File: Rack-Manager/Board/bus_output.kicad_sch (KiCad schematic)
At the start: 28 parts, among them J3 TBP03R1-350-04BE, J4 TBP03R1-350-04BE, Q1 NTR4003NT1G, Q2 SiS435DNT, Q3 NTR4003NT1G, Q4 SiS435DNT, U10 INA3221

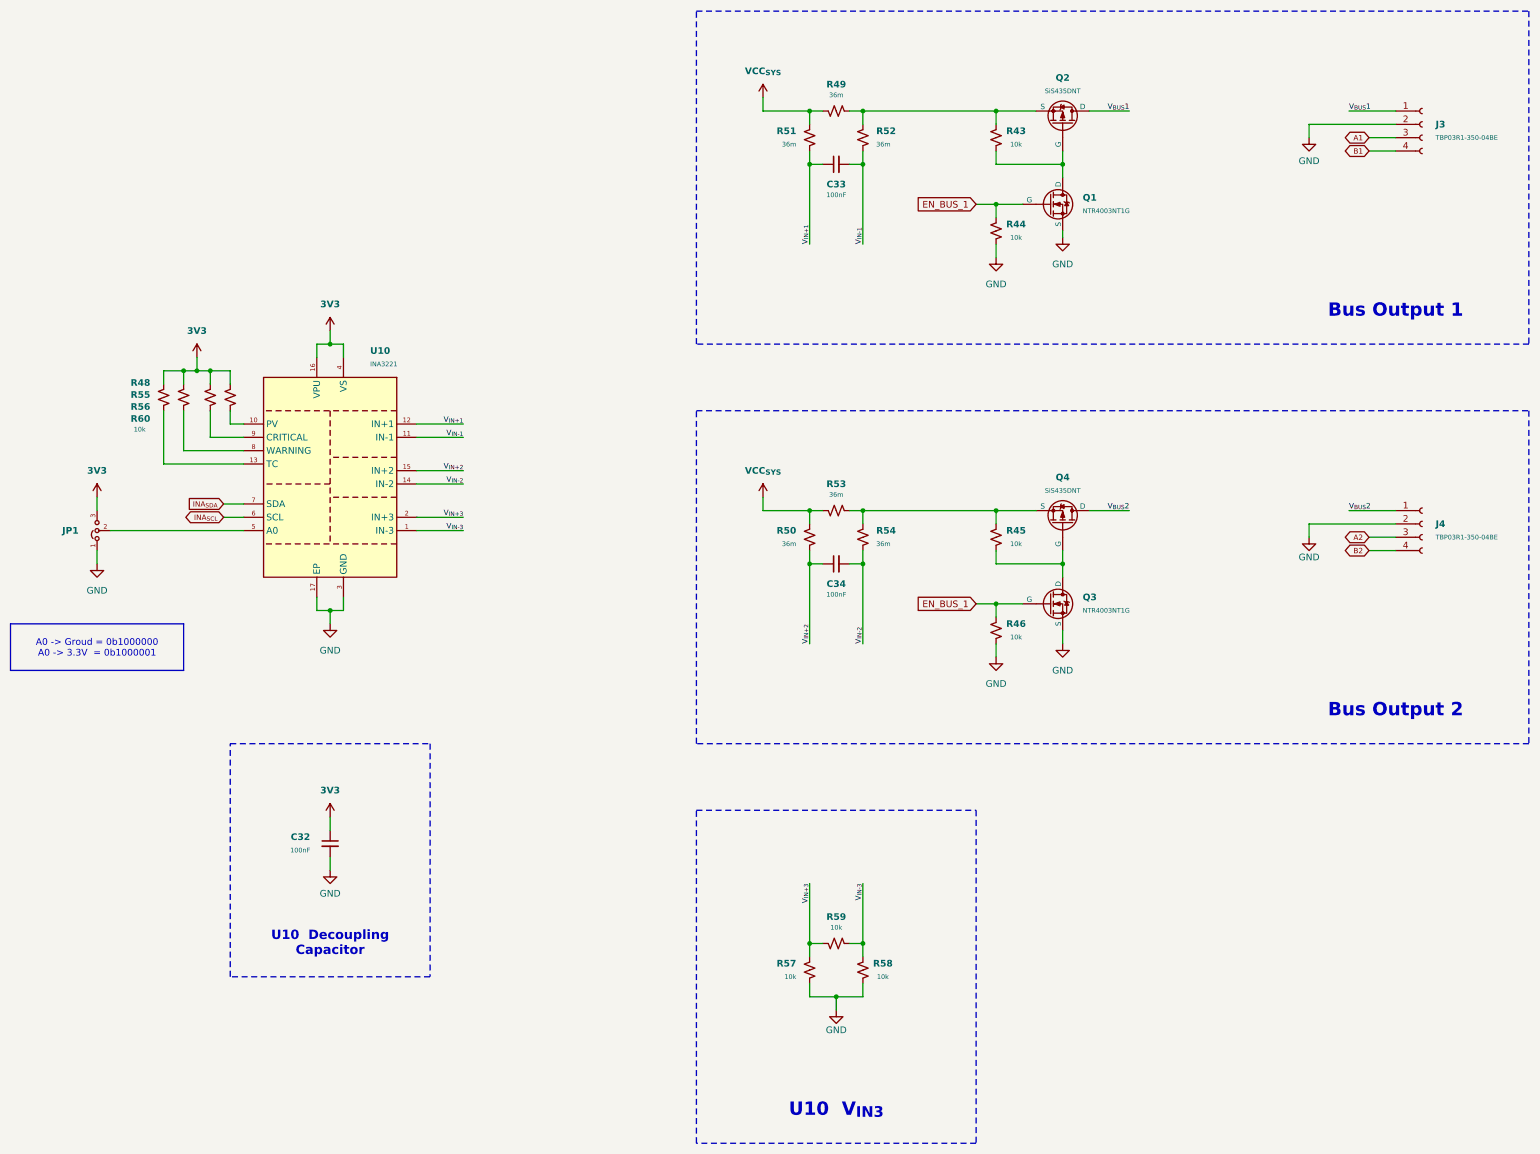
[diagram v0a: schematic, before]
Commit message: Added the fan management sheet and the mosfets for it
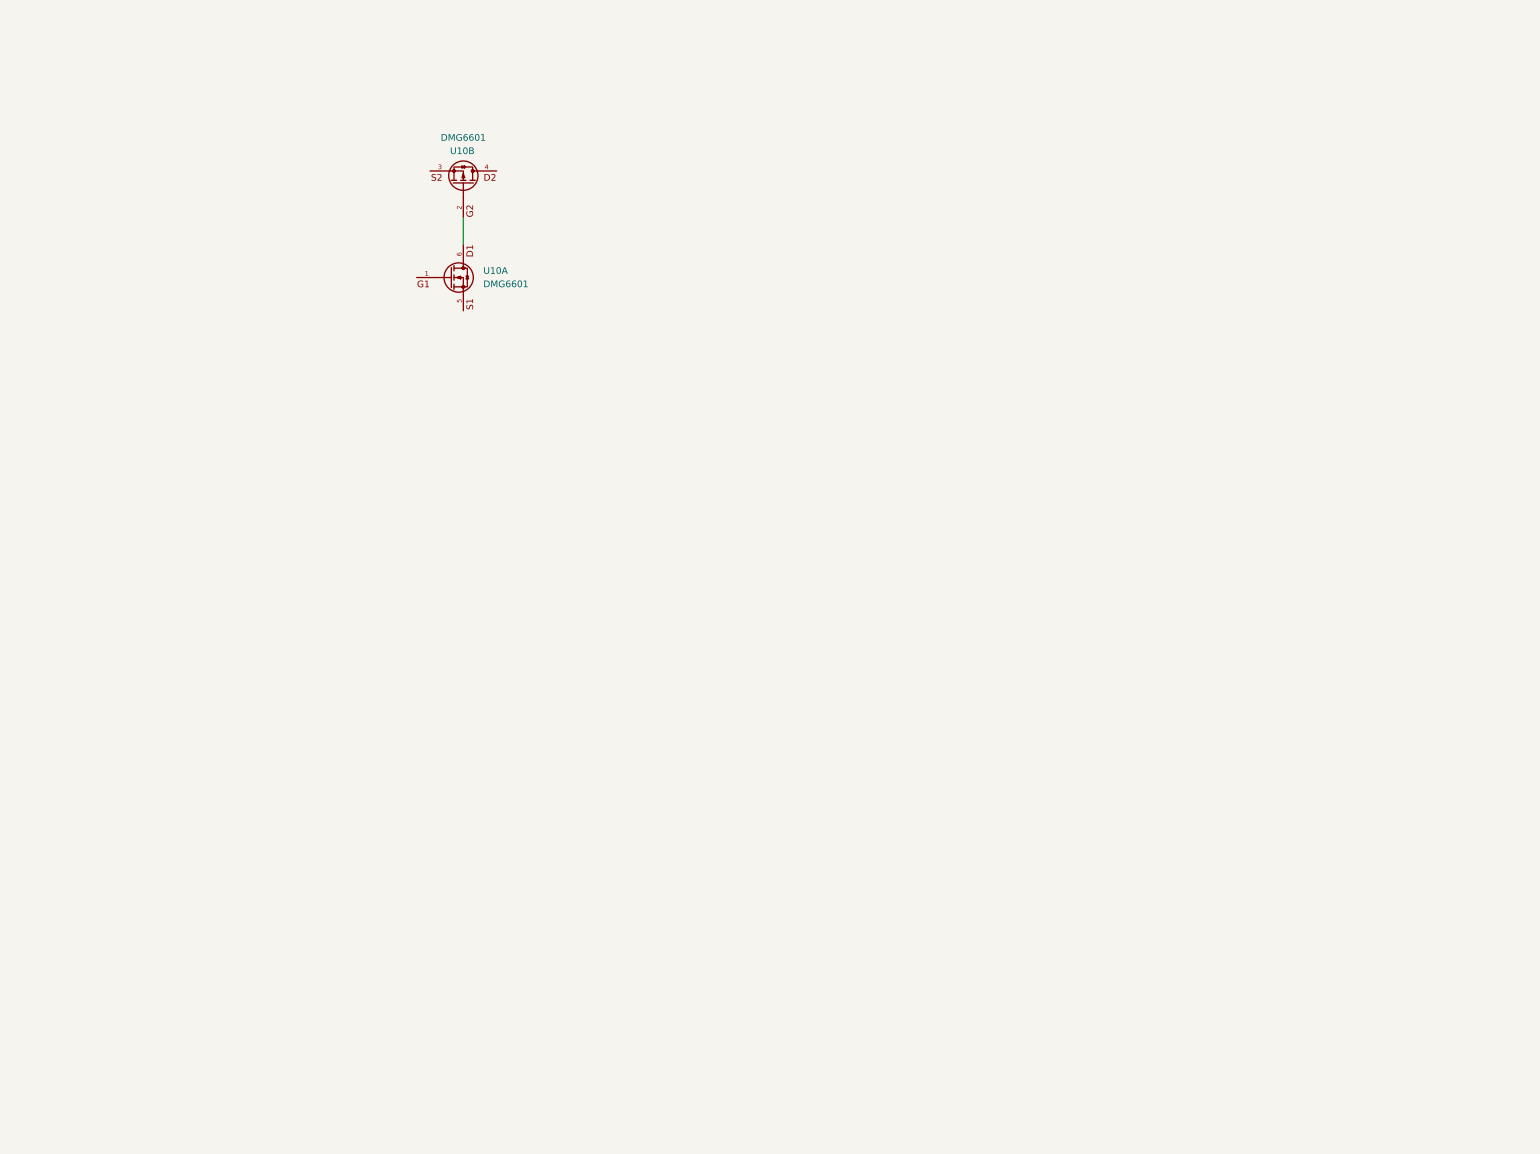
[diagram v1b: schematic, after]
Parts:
- removed C32, C33, C34: 100nF, Capacitor_SMD:C_0402_1005Metric, symbol Device:C_Small
- removed J3, J4: TBP03R1-350-04BE, Same Sky:TBP03R1-350-04BE, symbol Connector:Conn_01x04_Socket
- removed JP1: Jumper_3_Bridged12, TestPoint:TestPoint_2Pads_Pitch5.08mm_Drill1.3mm, symbol Jumper:Jumper_3_Bridged12
- removed Q1, Q3: NTR4003NT1G, Package_TO_SOT_SMD:SOT-23-3, symbol Simulation_SPICE:NMOS
- removed Q2, Q4: SiS435DNT, symbol Simulation_SPICE:PMOS
- removed R43, R44, R45, R46, R48, R55, R56, R57, R58, R60: 10k, Resistor_SMD:R_0201_0603Metric, symbol Device:R_Small_US
- removed R49, R50, R51, R52, R53, R54: 36m, symbol Device:R_Small_US
- removed R59: 10k, Resistor_SMD:R_0402_1005Metric, symbol Device:R_Small_US
- removed U10: INA3221, Package_DFN_QFN:Texas_RGV0016A_VQFN-16-1EP_4x4mm_P0.65mm_EP2.1x2.1mm, symbol Power_Management:INA3221
- added U10: DMG6601, symbol Diodes:DMG6601
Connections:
- new net: U10.2, U10.6
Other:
- note removed: "Bus Output 1"
- note removed: "Bus Output 2"
- note removed: "U10 Decoupling Capacitor"
- note removed: "U10 V_{IN3}"
